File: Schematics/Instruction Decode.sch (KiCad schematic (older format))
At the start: 10 parts

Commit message: annotate
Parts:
- gave numbers to parts that had none: 10
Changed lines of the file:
@@
 P 2900 1250
 AR Path="/5D2C0AA0/5DB5EC09" Ref="U?"  Part="1"
-AR Path="/5D2C0B92/5DB5EC09" Ref="U?"  Part="1"
-F 0 "U?" H 2550 1450 50  0000 C CNN
+AR Path="/5D2C0B92/5DB5EC09" Ref="U52"  Part="1"
+F 0 "U52" H 2550 1450 50  0000 C CNN
 F 1 "GLS29EE010" H 2550 1350 50  0000 C CNN
 F 2 "" H 2900 1250 50  0001 C CNN
@@
 P 2900 4200
 AR Path="/5D2C0AA0/5DB5EC5B" Ref="U?"  Part="1"
-AR Path="/5D2C0B92/5DB5EC5B" Ref="U?"  Part="1"
-F 0 "U?" H 2550 4400 50  0000 C CNN
+AR Path="/5D2C0B92/5DB5EC5B" Ref="U53"  Part="1"
+F 0 "U53" H 2550 4400 50  0000 C CNN
 F 1 "GLS29EE010" H 2550 4300 50  0000 C CNN
 F 2 "" H 2900 4200 50  0001 C CNN
@@
 P 8150 4950
 AR Path="/5D2C14C3/5DB613F7" Ref="U?"  Part="1"
-AR Path="/5D2C0B92/5DB613F7" Ref="U?"  Part="1"
-F 0 "U?" H 7900 5750 50  0000 C CNN
+AR Path="/5D2C0B92/5DB613F7" Ref="U56"  Part="1"
+F 0 "U56" H 7900 5750 50  0000 C CNN
 F 1 "74F574" H 7900 5650 50  0000 C CNN
 F 2 "" H 8150 4950 50  0001 C CNN
@@
 $EndComp
 $Comp
-L power:GND #PWR?
+L power:GND #PWR0213
 U 1 1 5DB6758A
 P 8150 5750
-F 0 "#PWR?" H 8150 5500 50  0001 C CNN
+F 0 "#PWR0213" H 8150 5500 50  0001 C CNN
 F 1 "GND" H 8155 5577 50  0000 C CNN
 F 2 "" H 8150 5750 50  0001 C CNN
@@
 $EndComp
 $Comp
-L power:VCC #PWR?
+L power:VCC #PWR0214
 U 1 1 5DB6804E
 P 8150 4150
-F 0 "#PWR?" H 8150 4000 50  0001 C CNN
+F 0 "#PWR0214" H 8150 4000 50  0001 C CNN
 F 1 "VCC" H 8167 4323 50  0000 C CNN
 F 2 "" H 8150 4150 50  0001 C CNN
@@
 ControlClock
 $Comp
-L power:GND #PWR?
+L power:GND #PWR0215
 U 1 1 5DB73C30
 P 7650 5450
-F 0 "#PWR?" H 7650 5200 50  0001 C CNN
+F 0 "#PWR0215" H 7650 5200 50  0001 C CNN
 F 1 "GND" V 7655 5322 50  0000 R CNN
 F 2 "" H 7650 5450 50  0001 C CNN
@@
 P 4400 1850
 AR Path="/5D2C14C3/5DB75B66" Ref="U?"  Part="1"
-AR Path="/5D2C0B92/5DB75B66" Ref="U?"  Part="1"
-F 0 "U?" H 4150 2650 50  0000 C CNN
+AR Path="/5D2C0B92/5DB75B66" Ref="U54"  Part="1"
+F 0 "U54" H 4150 2650 50  0000 C CNN
 F 1 "74F574" H 4150 2550 50  0000 C CNN
 F 2 "" H 4400 1850 50  0001 C CNN
@@
 P 4400 4800
 AR Path="/5D2C14C3/5DB7864A" Ref="U?"  Part="1"
-AR Path="/5D2C0B92/5DB7864A" Ref="U?"  Part="1"
-F 0 "U?" H 4150 5600 50  0000 C CNN
+AR Path="/5D2C0B92/5DB7864A" Ref="U55"  Part="1"
+F 0 "U55" H 4150 5600 50  0000 C CNN
 F 1 "74F574" H 4150 5500 50  0000 C CNN
 F 2 "" H 4400 4800 50  0001 C CNN
@@
 $EndComp
 $Comp
-L power:GND #PWR?
+L power:GND #PWR0216
 U 1 1 5DB796AD
 P 4400 5600
-F 0 "#PWR?" H 4400 5350 50  0001 C CNN
+F 0 "#PWR0216" H 4400 5350 50  0001 C CNN
 F 1 "GND" H 4405 5427 50  0000 C CNN
 F 2 "" H 4400 5600 50  0001 C CNN
@@
 $EndComp
 $Comp
-L power:GND #PWR?
+L power:GND #PWR0217
 U 1 1 5DB79B03
 P 4400 2650
-F 0 "#PWR?" H 4400 2400 50  0001 C CNN
+F 0 "#PWR0217" H 4400 2400 50  0001 C CNN
 F 1 "GND" H 4405 2477 50  0000 C CNN
 F 2 "" H 4400 2650 50  0001 C CNN
@@
 $EndComp
 $Comp
-L power:VCC #PWR?
+L power:VCC #PWR0218
 U 1 1 5DB7A069
 P 4400 1050
-F 0 "#PWR?" H 4400 900 50  0001 C CNN
+F 0 "#PWR0218" H 4400 900 50  0001 C CNN
 F 1 "VCC" H 4417 1223 50  0000 C CNN
 F 2 "" H 4400 1050 50  0001 C CNN
@@
 $EndComp
 $Comp
-L power:VCC #PWR?
+L power:VCC #PWR0219
 U 1 1 5DB7A788
 P 4400 4000
-F 0 "#PWR?" H 4400 3850 50  0001 C CNN
+F 0 "#PWR0219" H 4400 3850 50  0001 C CNN
 F 1 "VCC" H 4417 4173 50  0000 C CNN
 F 2 "" H 4400 4000 50  0001 C CNN
@@
 $EndComp
 $Comp
-L power:VCC #PWR?
+L power:VCC #PWR0220
 U 1 1 5DB7ADC3
 P 2900 4100
-F 0 "#PWR?" H 2900 3950 50  0001 C CNN
+F 0 "#PWR0220" H 2900 3950 50  0001 C CNN
 F 1 "VCC" H 2917 4273 50  0000 C CNN
 F 2 "" H 2900 4100 50  0001 C CNN
@@
 $EndComp
 $Comp
-L power:VCC #PWR?
+L power:VCC #PWR0221
 U 1 1 5DB7B2F7
 P 2900 1150
-F 0 "#PWR?" H 2900 1000 50  0001 C CNN
+F 0 "#PWR0221" H 2900 1000 50  0001 C CNN
 F 1 "VCC" H 2917 1323 50  0000 C CNN
 F 2 "" H 2900 1150 50  0001 C CNN
@@
 $EndComp
 $Comp
-L power:GND #PWR?
+L power:GND #PWR0222
 U 1 1 5DB7B91A
 P 2900 6500
-F 0 "#PWR?" H 2900 6250 50  0001 C CNN
+F 0 "#PWR0222" H 2900 6250 50  0001 C CNN
 F 1 "GND" H 2905 6327 50  0000 C CNN
 F 2 "" H 2900 6500 50  0001 C CNN
@@
 Connection ~ 3600 5200
 $Comp
-L power:GND #PWR?
+L power:GND #PWR0223
 U 1 1 5DB80A57
 P 3900 5300
-F 0 "#PWR?" H 3900 5050 50  0001 C CNN
+F 0 "#PWR0223" H 3900 5050 50  0001 C CNN
 F 1 "GND" V 3905 5172 50  0000 R CNN
 F 2 "" H 3900 5300 50  0001 C CNN
@@
 $EndComp
 $Comp
-L power:GND #PWR?
+L power:GND #PWR0224
 U 1 1 5DB8100B
 P 3900 2350
-F 0 "#PWR?" H 3900 2100 50  0001 C CNN
+F 0 "#PWR0224" H 3900 2100 50  0001 C CNN
 F 1 "GND" V 3905 2222 50  0000 R CNN
 F 2 "" H 3900 2350 50  0001 C CNN
@@
 	2200 6300 2250 6300
 $Comp
-L power:GND #PWR?
+L power:GND #PWR0225
 U 1 1 5DBD4428
 P 2200 6250
-F 0 "#PWR?" H 2200 6000 50  0001 C CNN
+F 0 "#PWR0225" H 2200 6000 50  0001 C CNN
 F 1 "GND" V 2205 6122 50  0000 R CNN
 F 2 "" H 2200 6250 50  0001 C CNN
@@
 	2200 3350 2250 3350
 $Comp
-L power:GND #PWR?
+L power:GND #PWR0226
 U 1 1 5DBE64D4
 P 2200 3300
-F 0 "#PWR?" H 2200 3050 50  0001 C CNN
+F 0 "#PWR0226" H 2200 3050 50  0001 C CNN
 F 1 "GND" V 2205 3172 50  0000 R CNN
 F 2 "" H 2200 3300 50  0001 C CNN
@@
 	2200 3300 2200 3350
 $Comp
-L power:VCC #PWR?
+L power:VCC #PWR0227
 U 1 1 5DBEAA53
 P 2200 6100
-F 0 "#PWR?" H 2200 5950 50  0001 C CNN
+F 0 "#PWR0227" H 2200 5950 50  0001 C CNN
 F 1 "VCC" V 2218 6227 50  0000 L CNN
 F 2 "" H 2200 6100 50  0001 C CNN
@@
 	2250 6100 2200 6100
 $Comp
-L power:VCC #PWR?
+L power:VCC #PWR0228
 U 1 1 5DBEFE69
 P 2200 3150
-F 0 "#PWR?" H 2200 3000 50  0001 C CNN
+F 0 "#PWR0228" H 2200 3000 50  0001 C CNN
 F 1 "VCC" V 2218 3277 50  0000 L CNN
 F 2 "" H 2200 3150 50  0001 C CNN
@@
 	2200 2450 2200 2550
 $Comp
-L power:GND #PWR?
+L power:GND #PWR0229
 U 1 1 5DC141C5
 P 2200 2850
-F 0 "#PWR?" H 2200 2600 50  0001 C CNN
+F 0 "#PWR0229" H 2200 2600 50  0001 C CNN
 F 1 "GND" V 2205 2722 50  0000 R CNN
 F 2 "" H 2200 2850 50  0001 C CNN
@@
 	2200 5400 2200 5500
 $Comp
-L power:GND #PWR?
+L power:GND #PWR0230
 U 1 1 5DC266E6
 P 2200 5800
-F 0 "#PWR?" H 2200 5550 50  0001 C CNN
+F 0 "#PWR0230" H 2200 5550 50  0001 C CNN
 F 1 "GND" V 2205 5672 50  0000 R CNN
 F 2 "" H 2200 5800 50  0001 C CNN
@@
 	1650 2250 2250 2250
 $Comp
-L power:GND #PWR?
+L power:GND #PWR0231
 U 1 1 5DC7501F
 P 2900 3550
-F 0 "#PWR?" H 2900 3300 50  0001 C CNN
+F 0 "#PWR0231" H 2900 3300 50  0001 C CNN
 F 1 "GND" H 2905 3377 50  0000 C CNN
 F 2 "" H 2900 3550 50  0001 C CNN
@@
 P 6700 700
 AR Path="/5D2C0761/5DC56D8C" Ref="#PWR?"  Part="1"
-AR Path="/5D2C0B92/5DC56D8C" Ref="#PWR?"  Part="1"
-F 0 "#PWR?" H 6700 550 50  0001 C CNN
+AR Path="/5D2C0B92/5DC56D8C" Ref="#PWR0232"  Part="1"
+F 0 "#PWR0232" H 6700 550 50  0001 C CNN
 F 1 "VCC" H 6717 873 50  0000 C CNN
 F 2 "" H 6700 700 50  0001 C CNN
@@
 P 6700 1000
 AR Path="/5D2C0761/5DC56D86" Ref="#PWR?"  Part="1"
-AR Path="/5D2C0B92/5DC56D86" Ref="#PWR?"  Part="1"
-F 0 "#PWR?" H 6700 750 50  0001 C CNN
+AR Path="/5D2C0B92/5DC56D86" Ref="#PWR0233"  Part="1"
+F 0 "#PWR0233" H 6700 750 50  0001 C CNN
 F 1 "GND" H 6705 827 50  0000 C CNN
 F 2 "" H 6700 1000 50  0001 C CNN
@@
 P 8700 850
 AR Path="/5D2C0761/5DC56D80" Ref="C?"  Part="1"
-AR Path="/5D2C0B92/5DC56D80" Ref="C?"  Part="1"
-F 0 "C?" H 8815 896 50  0000 L CNN
+AR Path="/5D2C0B92/5DC56D80" Ref="C49"  Part="1"
+F 0 "C49" H 8815 896 50  0000 L CNN
 F 1 "100nF" H 8815 805 50  0000 L CNN
 F 2 "" H 8738 700 50  0001 C CNN
@@
 P 8200 850
 AR Path="/5D2C0761/5DC56D7A" Ref="C?"  Part="1"
-AR Path="/5D2C0B92/5DC56D7A" Ref="C?"  Part="1"
-F 0 "C?" H 8315 896 50  0000 L CNN
+AR Path="/5D2C0B92/5DC56D7A" Ref="C48"  Part="1"
+F 0 "C48" H 8315 896 50  0000 L CNN
 F 1 "100nF" H 8315 805 50  0000 L CNN
 F 2 "" H 8238 700 50  0001 C CNN
@@
 P 7700 850
 AR Path="/5D2C0761/5DC56D74" Ref="C?"  Part="1"
-AR Path="/5D2C0B92/5DC56D74" Ref="C?"  Part="1"
-F 0 "C?" H 7815 896 50  0000 L CNN
+AR Path="/5D2C0B92/5DC56D74" Ref="C47"  Part="1"
+F 0 "C47" H 7815 896 50  0000 L CNN
 F 1 "100nF" H 7815 805 50  0000 L CNN
 F 2 "" H 7738 700 50  0001 C CNN
@@
 P 7200 850
 AR Path="/5D2C0761/5DC56D6E" Ref="C?"  Part="1"
-AR Path="/5D2C0B92/5DC56D6E" Ref="C?"  Part="1"
-F 0 "C?" H 7315 896 50  0000 L CNN
+AR Path="/5D2C0B92/5DC56D6E" Ref="C46"  Part="1"
+F 0 "C46" H 7315 896 50  0000 L CNN
 F 1 "100nF" H 7315 805 50  0000 L CNN
 F 2 "" H 7238 700 50  0001 C CNN
@@
 P 6700 850
 AR Path="/5D2C0761/5DC56D68" Ref="C?"  Part="1"
-AR Path="/5D2C0B92/5DC56D68" Ref="C?"  Part="1"
-F 0 "C?" H 6815 896 50  0000 L CNN
+AR Path="/5D2C0B92/5DC56D68" Ref="C45"  Part="1"
+F 0 "C45" H 6815 896 50  0000 L CNN
 F 1 "100nF" H 6815 805 50  0000 L CNN
 F 2 "" H 6738 700 50  0001 C CNN

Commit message: Assign a bunch of part footprints.
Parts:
- C45, C46, C47, C48, C49: footprint (none) -> Capacitor_THT:C_Disc_D4.3mm_W1.9mm_P5.00mm
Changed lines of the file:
@@
 F 0 "C49" H 8815 896 50  0000 L CNN
 F 1 "100nF" H 8815 805 50  0000 L CNN
-F 2 "" H 8738 700 50  0001 C CNN
+F 2 "Capacitor_THT:C_Disc_D4.3mm_W1.9mm_P5.00mm" H 8738 700 50  0001 C CNN
 F 3 "~" H 8700 850 50  0001 C CNN
 	1    8700 850
@@
 F 0 "C48" H 8315 896 50  0000 L CNN
 F 1 "100nF" H 8315 805 50  0000 L CNN
-F 2 "" H 8238 700 50  0001 C CNN
+F 2 "Capacitor_THT:C_Disc_D4.3mm_W1.9mm_P5.00mm" H 8238 700 50  0001 C CNN
 F 3 "~" H 8200 850 50  0001 C CNN
 	1    8200 850
@@
 F 0 "C47" H 7815 896 50  0000 L CNN
 F 1 "100nF" H 7815 805 50  0000 L CNN
-F 2 "" H 7738 700 50  0001 C CNN
+F 2 "Capacitor_THT:C_Disc_D4.3mm_W1.9mm_P5.00mm" H 7738 700 50  0001 C CNN
 F 3 "~" H 7700 850 50  0001 C CNN
 	1    7700 850
@@
 F 0 "C46" H 7315 896 50  0000 L CNN
 F 1 "100nF" H 7315 805 50  0000 L CNN
-F 2 "" H 7238 700 50  0001 C CNN
+F 2 "Capacitor_THT:C_Disc_D4.3mm_W1.9mm_P5.00mm" H 7238 700 50  0001 C CNN
 F 3 "~" H 7200 850 50  0001 C CNN
 	1    7200 850
@@
 F 0 "C45" H 6815 896 50  0000 L CNN
 F 1 "100nF" H 6815 805 50  0000 L CNN
-F 2 "" H 6738 700 50  0001 C CNN
+F 2 "Capacitor_THT:C_Disc_D4.3mm_W1.9mm_P5.00mm" H 6738 700 50  0001 C CNN
 F 3 "~" H 6700 850 50  0001 C CNN
 	1    6700 850

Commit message: Assign a bunch more footprints. All are assigned now.
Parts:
- U52, U53: footprint (none) -> Package_DIP:DIP-32_W15.24mm_Socket
- U54, U55, U56: footprint (none) -> Package_DIP:DIP-20_W7.62mm
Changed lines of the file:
@@
 F 0 "U52" H 2550 1450 50  0000 C CNN
 F 1 "GLS29EE010" H 2550 1350 50  0000 C CNN
-F 2 "" H 2900 1250 50  0001 C CNN
+F 2 "Package_DIP:DIP-32_W15.24mm_Socket" H 2900 1250 50  0001 C CNN
 F 3 "" H 2900 1250 50  0001 C CNN
 	1    2900 1250
@@
 F 0 "U53" H 2550 4400 50  0000 C CNN
 F 1 "GLS29EE010" H 2550 4300 50  0000 C CNN
-F 2 "" H 2900 4200 50  0001 C CNN
+F 2 "Package_DIP:DIP-32_W15.24mm_Socket" H 2900 4200 50  0001 C CNN
 F 3 "" H 2900 4200 50  0001 C CNN
 	1    2900 4200
@@
 F 0 "U56" H 7900 5750 50  0000 C CNN
 F 1 "74F574" H 7900 5650 50  0000 C CNN
-F 2 "" H 8150 4950 50  0001 C CNN
+F 2 "Package_DIP:DIP-20_W7.62mm" H 8150 4950 50  0001 C CNN
 F 3 "http://www.ti.com/lit/gpn/sn74LS574" H 8150 4950 50  0001 C CNN
 	1    8150 4950
@@
 F 0 "U54" H 4150 2650 50  0000 C CNN
 F 1 "74F574" H 4150 2550 50  0000 C CNN
-F 2 "" H 4400 1850 50  0001 C CNN
+F 2 "Package_DIP:DIP-20_W7.62mm" H 4400 1850 50  0001 C CNN
 F 3 "http://www.ti.com/lit/gpn/sn74LS574" H 4400 1850 50  0001 C CNN
 	1    4400 1850
@@
 F 0 "U55" H 4150 5600 50  0000 C CNN
 F 1 "74F574" H 4150 5500 50  0000 C CNN
-F 2 "" H 4400 4800 50  0001 C CNN
+F 2 "Package_DIP:DIP-20_W7.62mm" H 4400 4800 50  0001 C CNN
 F 3 "http://www.ti.com/lit/gpn/sn74LS574" H 4400 4800 50  0001 C CNN
 	1    4400 4800

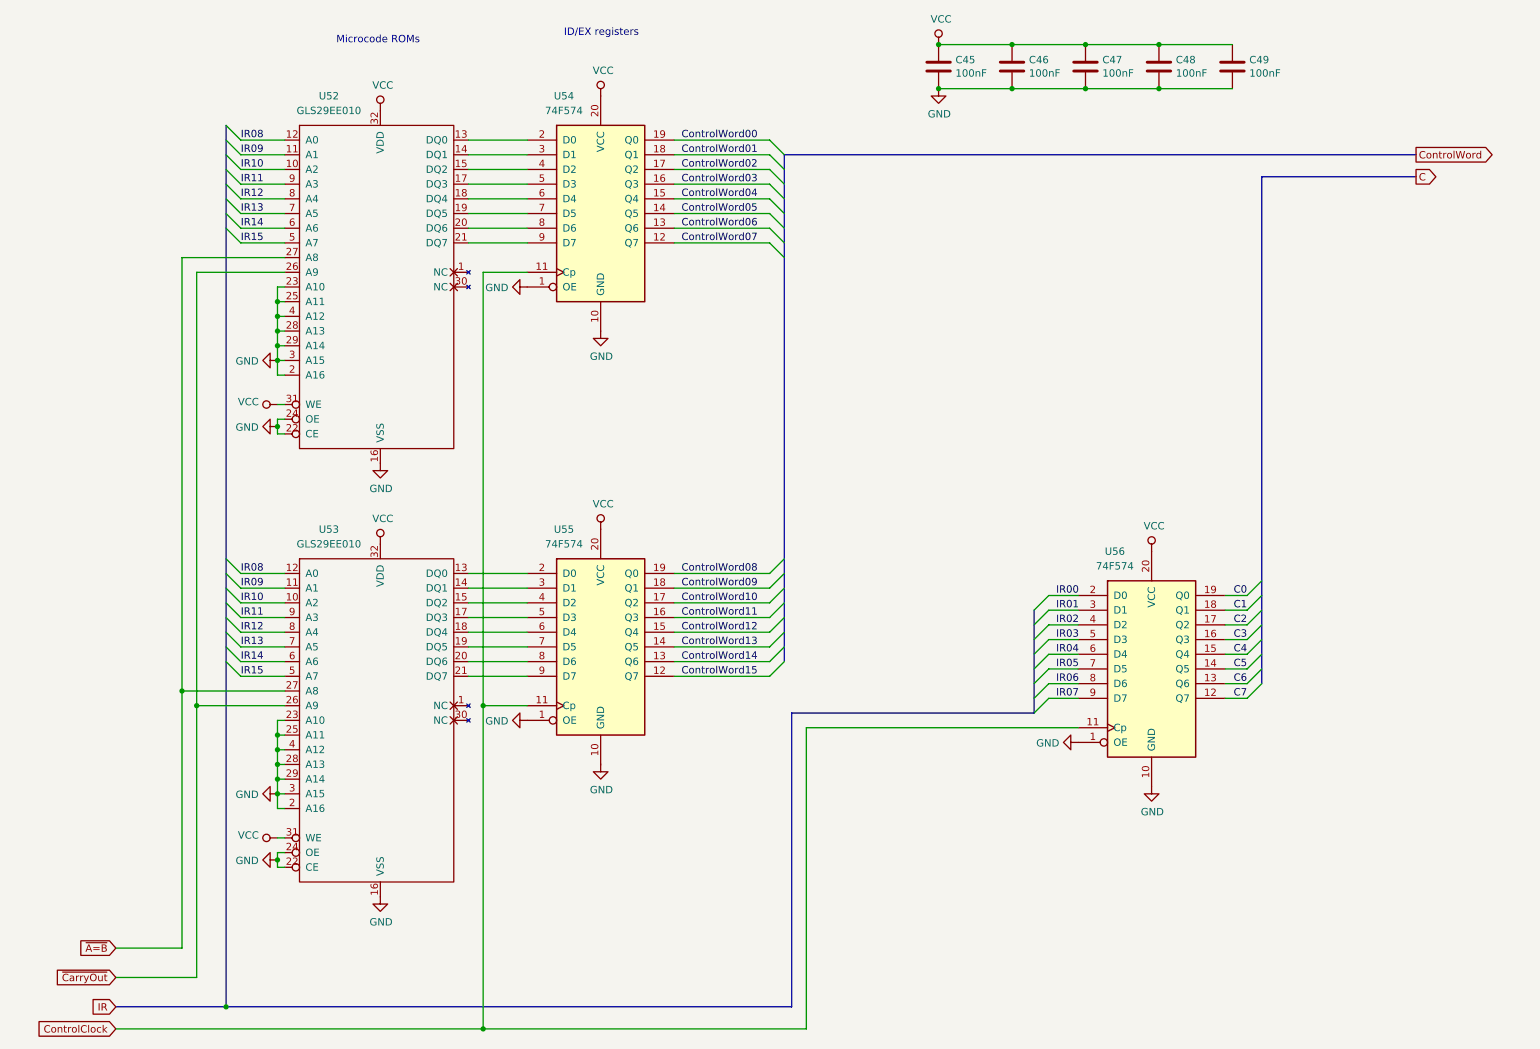
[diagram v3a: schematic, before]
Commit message: My buses were not named according the rules in the Eeschema manual.
Buses which connect to global labels must be named specially.
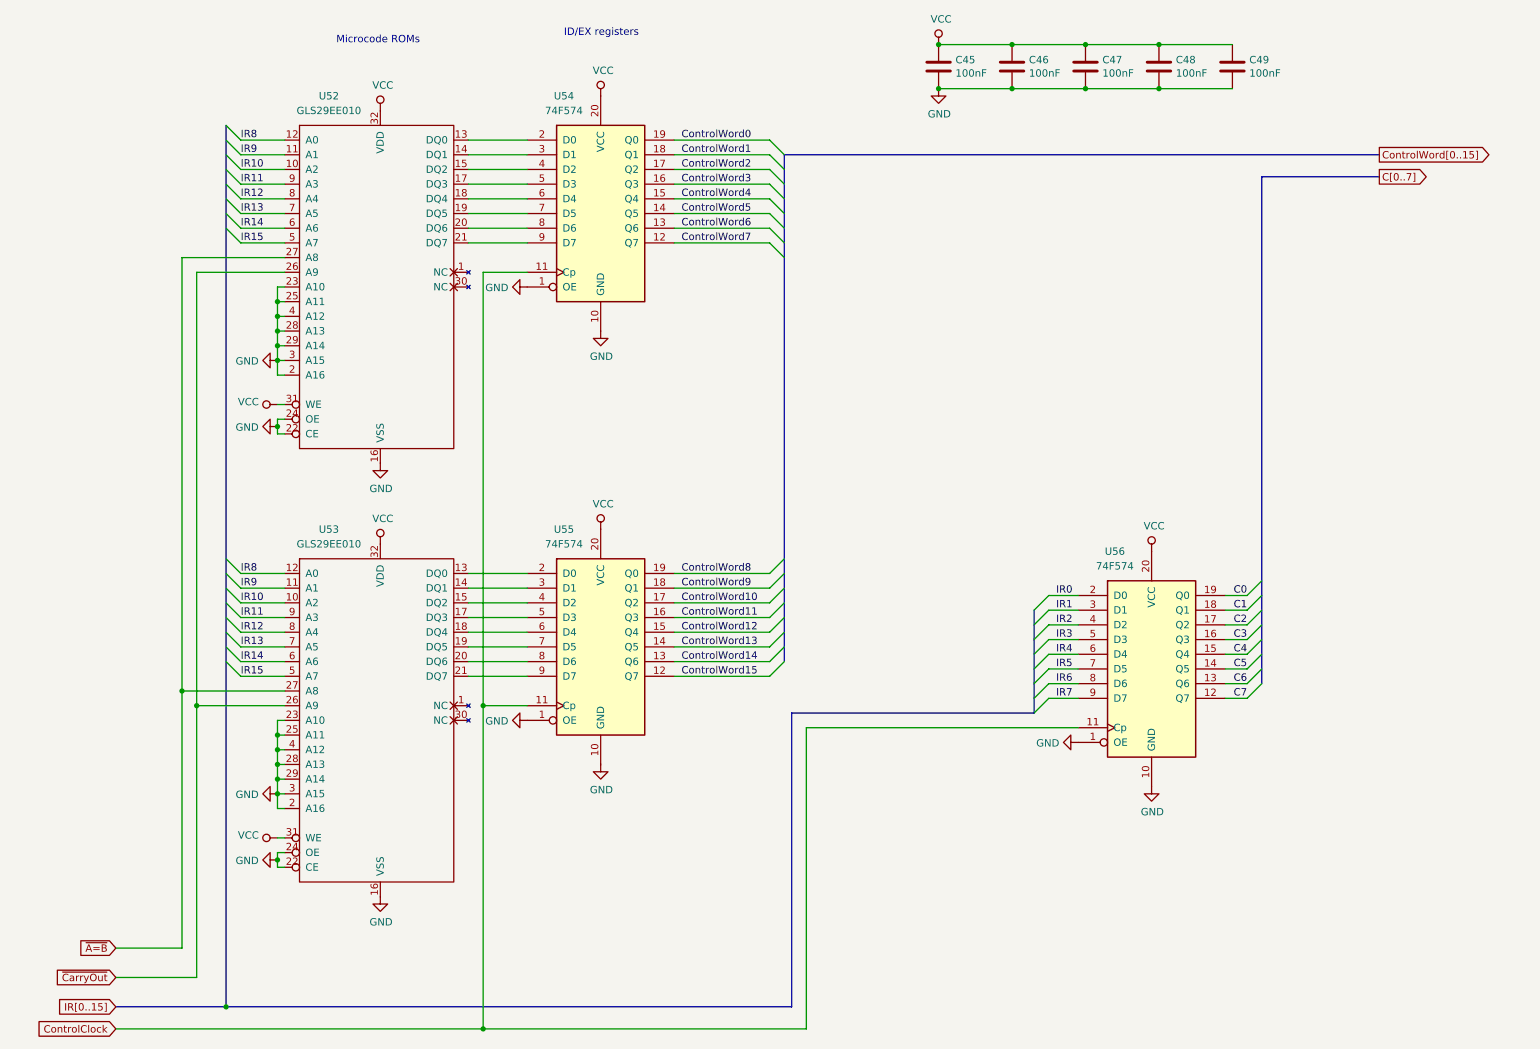
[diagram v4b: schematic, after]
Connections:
- net ControlWord00 renamed ControlWord0
- net ControlWord01 renamed ControlWord1
- net ControlWord02 renamed ControlWord2
- net ControlWord03 renamed ControlWord3
- net ControlWord04 renamed ControlWord4
- net ControlWord05 renamed ControlWord5
- net ControlWord06 renamed ControlWord6
- net ControlWord07 renamed ControlWord7
- net ControlWord08 renamed ControlWord8
- net ControlWord09 renamed ControlWord9
- net IR00 renamed IR0
- net IR01 renamed IR1
- net IR02 renamed IR2
- net IR03 renamed IR3
- net IR04 renamed IR4
- net IR05 renamed IR5
- net IR06 renamed IR6
- net IR07 renamed IR7
- net IR08 renamed IR8
- net IR09 renamed IR9
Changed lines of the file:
@@
 	7650 4450 7450 4450
 Text GLabel 1100 7250 0    50   Input ~ 0
-IR
+IR[0..15]
 Text Label 7500 4450 0    50   ~ 0
-IR00
+IR0
 Text Label 7500 4550 0    50   ~ 0
-IR01
+IR1
 Text Label 7500 4650 0    50   ~ 0
-IR02
+IR2
 Text Label 7500 4750 0    50   ~ 0
-IR03
+IR3
 Text Label 7500 4850 0    50   ~ 0
-IR04
+IR4
 Text Label 7500 4950 0    50   ~ 0
-IR05
+IR5
 Text Label 7500 5050 0    50   ~ 0
-IR06
+IR6
 Text Label 7500 5150 0    50   ~ 0
-IR07
+IR7
 Text GLabel 1100 7400 0    50   Input ~ 0
 ControlClock
@@
 	2250 5000 1950 5000
 Text Label 1950 4300 0    50   ~ 0
-IR08
+IR8
 Text Label 1950 4400 0    50   ~ 0
-IR09
+IR9
 Text Label 1950 4500 0    50   ~ 0
 IR10
@@
 	2250 2050 1950 2050
 Text Label 1950 1350 0    50   ~ 0
-IR08
+IR8
 Text Label 1950 1450 0    50   ~ 0
-IR09
+IR9
 Text Label 1950 1550 0    50   ~ 0
 IR10
@@
 Microcode ROMs
 Text Label 4950 1350 0    50   ~ 0
-ControlWord00
+ControlWord0
 Text Label 4950 1450 0    50   ~ 0
-ControlWord01
+ControlWord1
 Text Label 4950 1550 0    50   ~ 0
-ControlWord02
+ControlWord2
 Text Label 4950 1650 0    50   ~ 0
-ControlWord03
+ControlWord3
 Text Label 4950 1750 0    50   ~ 0
-ControlWord04
+ControlWord4
 Text Label 4950 1850 0    50   ~ 0
-ControlWord05
+ControlWord5
 Text Label 4950 1950 0    50   ~ 0
-ControlWord06
+ControlWord6
 Text Label 4950 2050 0    50   ~ 0
-ControlWord07
+ControlWord7
 Wire Wire Line
 	4900 4800 5550 4800
@@
 	4900 4300 5550 4300
 Text Label 4950 4300 0    50   ~ 0
-ControlWord08
+ControlWord8
 Text Label 4950 4400 0    50   ~ 0
-ControlWord09
+ControlWord9
 Text Label 4950 4500 0    50   ~ 0
 ControlWord10
@@
 Entry Wire Line
 	5550 1350 5650 1450
-Text GLabel 9950 1450 2    50   Output ~ 0
-ControlWord
+Text GLabel 9700 1450 2    50   Output ~ 0
+ControlWord[0..15]
 Wire Bus Line
-	5650 1450 9950 1450
+	5650 1450 9700 1450
 Entry Wire Line
 	8800 5150 8900 5050
@@
 Entry Wire Line
 	8800 4450 8900 4350
-Text GLabel 9950 1600 2    50   Output ~ 0
-C
+Text GLabel 9700 1600 2    50   Output ~ 0
+C[0..7]
 Text Label 8800 4450 2    50   ~ 0
 C0
@@
 	5800 5350 5800 7400
 Wire Bus Line
-	8900 1600 9950 1600
+	8900 1600 9700 1600
 Wire Bus Line
 	5700 5250 7350 5250
